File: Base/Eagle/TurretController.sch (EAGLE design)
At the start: 88 parts, among them CN1 2EDG-2, IC1 LM2596S-5, IC2 MCP23017SO, Q1 BC818-16SMD, Q2 BC818-16SMD, Q3 BC818-16SMD, Q4 BC818-16SMD

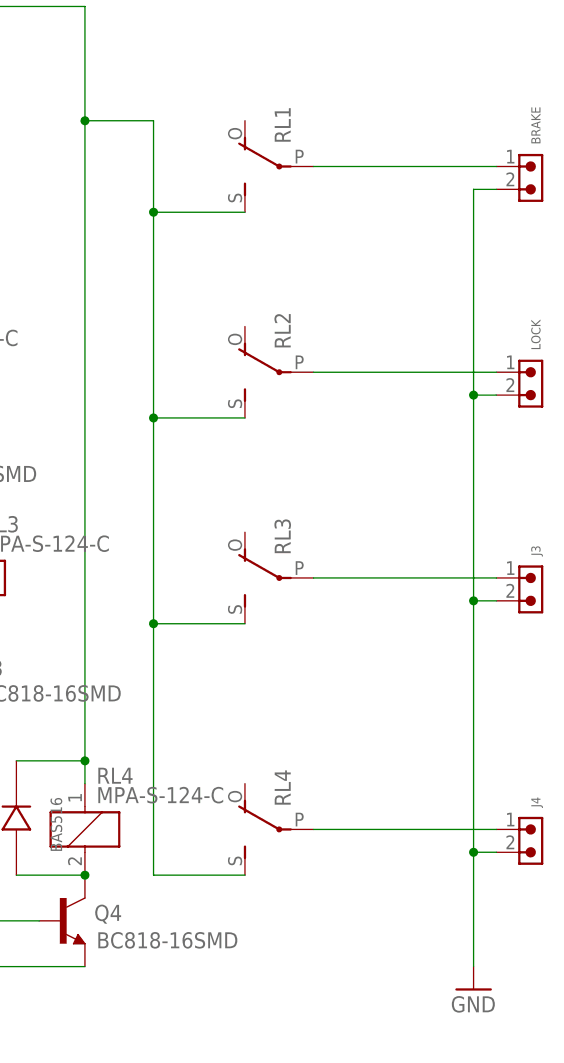
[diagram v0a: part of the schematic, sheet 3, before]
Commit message: First corrections to board, addition of protection diodes
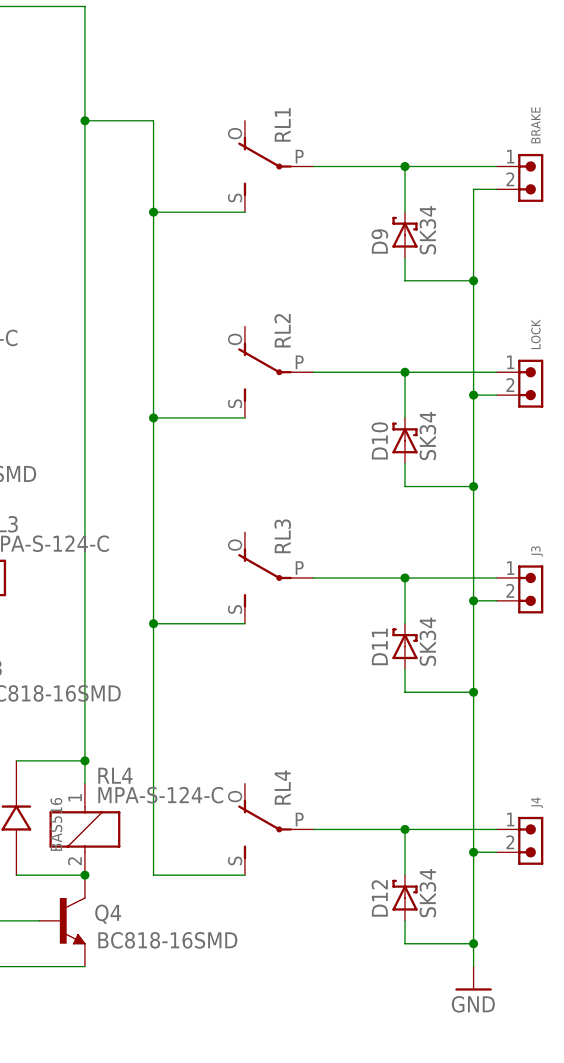
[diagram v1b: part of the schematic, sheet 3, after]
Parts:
- added D10, D11, D12, D9: SK34, Diodes:SK34
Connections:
- net N$10 renamed STEP
- net N$8 renamed DIR
- net GND: now also D10.A, D11.A, D12.A, D9.A, OK4B.C
- net N$11: now also D9.C
- net N$3: now also D12.C
- net N$4: now also D11.C
- net N$9: now also D10.C
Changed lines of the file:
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@@
 </part>
 <part name="R39" library="rcl" library_urn="urn:adsk.eagle:library:334" deviceset="R-EU_" device="R0805" package3d_urn="urn:adsk.eagle:package:23553/2"/>
+<part name="D9" library="Diodes" deviceset="SK34" device="" value="SK34">
+<attribute name="SPICEPREFIX" value="D"/>
+</part>
+<part name="D10" library="Diodes" deviceset="SK34" device="" value="SK34">
+<attribute name="SPICEPREFIX" value="D"/>
+</part>
+<part name="D11" library="Diodes" deviceset="SK34" device="" value="SK34">
+<attribute name="SPICEPREFIX" value="D"/>
+</part>
+<part name="D12" library="Diodes" deviceset="SK34" device="" value="SK34">
+<attribute name="SPICEPREFIX" value="D"/>
+</part>
 </parts>
 <sheets>
@@
 </segment>
 </net>
-<net name="N$8" class="0">
+<net name="DIR" class="0">
 <segment>
 <pinref part="U$1" gate="G$1" pin="D12"/>
@@
 <wire x1="162.56" y1="160.02" x2="162.56" y2="134.62" width="0.1524" layer="91"/>
 <wire x1="154.94" y1="134.62" x2="162.56" y2="134.62" width="0.1524" layer="91"/>
-</segment>
-</net>
-<net name="N$10" class="0">
+<label x="162.56" y="142.24" size="1.778" layer="95" rot="R90"/>
+</segment>
+</net>
+<net name="STEP" class="0">
 <segment>
 <pinref part="U$1" gate="G$1" pin="D11"/>
@@
 <wire x1="157.48" y1="160.02" x2="157.48" y2="132.08" width="0.1524" layer="91"/>
 <wire x1="157.48" y1="132.08" x2="154.94" y2="132.08" width="0.1524" layer="91"/>
+<label x="157.48" y="142.24" size="1.778" layer="95" rot="R90"/>
 </segment>
 </net>
@@
 <attribute name="VALUE" x="233.68" y="71.12" size="1.778" layer="96"/>
 </instance>
+<instance part="D9" gate="G$1" x="228.6" y="157.48" smashed="yes" rot="R90">
+<attribute name="NAME" x="226.695" y="155.194" size="1.778" layer="95" rot="R90"/>
+<attribute name="VALUE" x="232.029" y="155.194" size="1.778" layer="96" rot="R90"/>
+</instance>
+<instance part="D10" gate="G$1" x="228.6" y="134.62" smashed="yes" rot="R90">
+<attribute name="NAME" x="226.695" y="132.334" size="1.778" layer="95" rot="R90"/>
+<attribute name="VALUE" x="232.029" y="132.334" size="1.778" layer="96" rot="R90"/>
+</instance>
+<instance part="D11" gate="G$1" x="228.6" y="111.76" smashed="yes" rot="R90">
+<attribute name="NAME" x="226.695" y="109.474" size="1.778" layer="95" rot="R90"/>
+<attribute name="VALUE" x="232.029" y="109.474" size="1.778" layer="96" rot="R90"/>
+</instance>
+<instance part="D12" gate="G$1" x="228.6" y="83.82" smashed="yes" rot="R90">
+<attribute name="NAME" x="226.695" y="81.534" size="1.778" layer="95" rot="R90"/>
+<attribute name="VALUE" x="232.029" y="81.534" size="1.778" layer="96" rot="R90"/>
+</instance>
 </instances>
 <busses>
@@
 <segment>
 <pinref part="RL4" gate="G$2" pin="P"/>
-<wire x1="238.76" y1="91.44" x2="218.44" y2="91.44" width="0.1524" layer="91"/>
+<wire x1="238.76" y1="91.44" x2="228.6" y2="91.44" width="0.1524" layer="91"/>
 <pinref part="J4" gate="G$1" pin="1"/>
+<pinref part="D12" gate="G$1" pin="C"/>
+<wire x1="228.6" y1="91.44" x2="218.44" y2="91.44" width="0.1524" layer="91"/>
+<wire x1="228.6" y1="86.36" x2="228.6" y2="91.44" width="0.1524" layer="91"/>
+<junction x="228.6" y="91.44"/>
 </segment>
 </net>
@@
 <segment>
 <pinref part="RL3" gate="G$2" pin="P"/>
-<wire x1="238.76" y1="119.38" x2="218.44" y2="119.38" width="0.1524" layer="91"/>
+<wire x1="238.76" y1="119.38" x2="228.6" y2="119.38" width="0.1524" layer="91"/>
 <pinref part="J3" gate="G$1" pin="1"/>
+<pinref part="D11" gate="G$1" pin="C"/>
+<wire x1="228.6" y1="119.38" x2="218.44" y2="119.38" width="0.1524" layer="91"/>
+<wire x1="228.6" y1="114.3" x2="228.6" y2="119.38" width="0.1524" layer="91"/>
+<junction x="228.6" y="119.38"/>
 </segment>
 </net>
@@
 <segment>
 <pinref part="RL2" gate="G$2" pin="P"/>
-<wire x1="238.76" y1="142.24" x2="218.44" y2="142.24" width="0.1524" layer="91"/>
+<wire x1="238.76" y1="142.24" x2="228.6" y2="142.24" width="0.1524" layer="91"/>
 <pinref part="LOCK" gate="G$1" pin="1"/>
+<pinref part="D10" gate="G$1" pin="C"/>
+<wire x1="228.6" y1="142.24" x2="218.44" y2="142.24" width="0.1524" layer="91"/>
+<wire x1="228.6" y1="137.16" x2="228.6" y2="142.24" width="0.1524" layer="91"/>
+<junction x="228.6" y="142.24"/>
 </segment>
 </net>
@@
 <segment>
 <pinref part="RL1" gate="G$2" pin="P"/>
-<wire x1="218.44" y1="165.1" x2="238.76" y2="165.1" width="0.1524" layer="91"/>
+<wire x1="218.44" y1="165.1" x2="228.6" y2="165.1" width="0.1524" layer="91"/>
 <pinref part="BRAKE" gate="G$1" pin="1"/>
+<pinref part="D9" gate="G$1" pin="C"/>
+<wire x1="228.6" y1="165.1" x2="238.76" y2="165.1" width="0.1524" layer="91"/>
+<wire x1="228.6" y1="160.02" x2="228.6" y2="165.1" width="0.1524" layer="91"/>
+<junction x="228.6" y="165.1"/>
 </segment>
 </net>
@@
 </segment>
 <segment>
-<wire x1="236.22" y1="76.2" x2="236.22" y2="88.9" width="0.1524" layer="91"/>
+<wire x1="236.22" y1="76.2" x2="236.22" y2="78.74" width="0.1524" layer="91"/>
 <pinref part="BRAKE" gate="G$1" pin="2"/>
-<wire x1="236.22" y1="88.9" x2="236.22" y2="116.84" width="0.1524" layer="91"/>
-<wire x1="236.22" y1="116.84" x2="236.22" y2="139.7" width="0.1524" layer="91"/>
-<wire x1="236.22" y1="139.7" x2="236.22" y2="162.56" width="0.1524" layer="91"/>
+<wire x1="236.22" y1="78.74" x2="236.22" y2="88.9" width="0.1524" layer="91"/>
+<wire x1="236.22" y1="88.9" x2="236.22" y2="106.68" width="0.1524" layer="91"/>
+<wire x1="236.22" y1="106.68" x2="236.22" y2="116.84" width="0.1524" layer="91"/>
+<wire x1="236.22" y1="116.84" x2="236.22" y2="129.54" width="0.1524" layer="91"/>
+<wire x1="236.22" y1="129.54" x2="236.22" y2="139.7" width="0.1524" layer="91"/>
+<wire x1="236.22" y1="139.7" x2="236.22" y2="152.4" width="0.1524" layer="91"/>
+<wire x1="236.22" y1="152.4" x2="236.22" y2="162.56" width="0.1524" layer="91"/>
 <wire x1="236.22" y1="162.56" x2="238.76" y2="162.56" width="0.1524" layer="91"/>
 <pinref part="LOCK" gate="G$1" pin="2"/>
@@
 <junction x="236.22" y="88.9"/>
 <pinref part="GND2" gate="1" pin="GND"/>
+<pinref part="D12" gate="G$1" pin="A"/>
+<wire x1="228.6" y1="81.28" x2="228.6" y2="78.74" width="0.1524" layer="91"/>
+<wire x1="228.6" y1="78.74" x2="236.22" y2="78.74" width="0.1524" layer="91"/>
+<junction x="236.22" y="78.74"/>
+<pinref part="D11" gate="G$1" pin="A"/>
+<wire x1="228.6" y1="109.22" x2="228.6" y2="106.68" width="0.1524" layer="91"/>
+<wire x1="228.6" y1="106.68" x2="236.22" y2="106.68" width="0.1524" layer="91"/>
+<junction x="236.22" y="106.68"/>
+<pinref part="D10" gate="G$1" pin="A"/>
+<wire x1="228.6" y1="132.08" x2="228.6" y2="129.54" width="0.1524" layer="91"/>
+<wire x1="228.6" y1="129.54" x2="236.22" y2="129.54" width="0.1524" layer="91"/>
+<junction x="236.22" y="129.54"/>
+<pinref part="D9" gate="G$1" pin="A"/>
+<wire x1="228.6" y1="154.94" x2="228.6" y2="152.4" width="0.1524" layer="91"/>
+<wire x1="228.6" y1="152.4" x2="236.22" y2="152.4" width="0.1524" layer="91"/>
+<junction x="236.22" y="152.4"/>
 </segment>
 </net>
@@
 <pinref part="OK4" gate="A" pin="C"/>
 <wire x1="165.1" y1="132.08" x2="162.56" y2="132.08" width="0.1524" layer="91"/>
-<wire x1="162.56" y1="132.08" x2="162.56" y2="96.52" width="0.1524" layer="91"/>
+<wire x1="162.56" y1="132.08" x2="162.56" y2="109.22" width="0.1524" layer="91"/>
 <pinref part="GND15" gate="1" pin="GND"/>
-</segment>
-</net>
+<pinref part="OK4" gate="B" pin="C"/>
+<wire x1="162.56" y1="109.22" x2="162.56" y2="96.52" width="0.1524" layer="91"/>
+<wire x1="165.1" y1="109.22" x2="162.56" y2="109.22" width="0.1524" layer="91"/>
+<junction x="162.56" y="109.22"/>
+</segment>
+</net>
